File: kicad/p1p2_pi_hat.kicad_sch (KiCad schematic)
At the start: 68 parts, among them J1 Raspberry_Pi_2_3, J2 PC MC_1,5_2-G-3.81, Q1 BSS123, SW1 SW_Push, U1 LM4040DBZ-3, U103 TS4990, U3 Pico

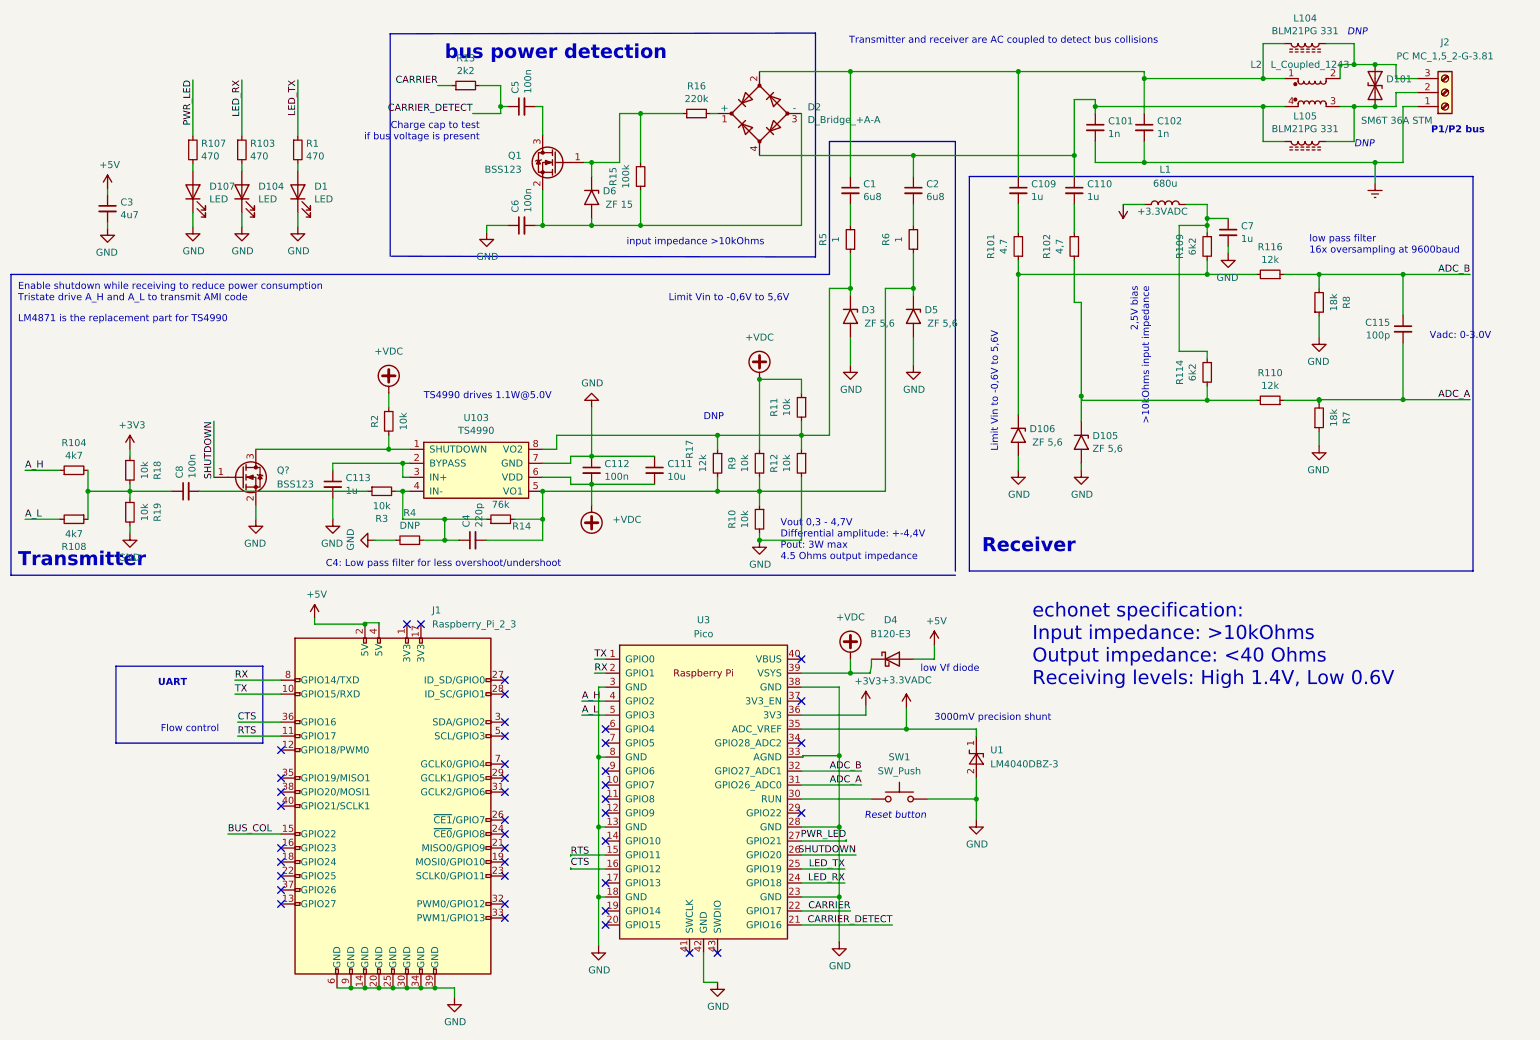
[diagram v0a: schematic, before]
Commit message: kicad: use DNP flag
Signed-off-by: Patrick Rudolph <rudolphpatrick05@gmail.com>
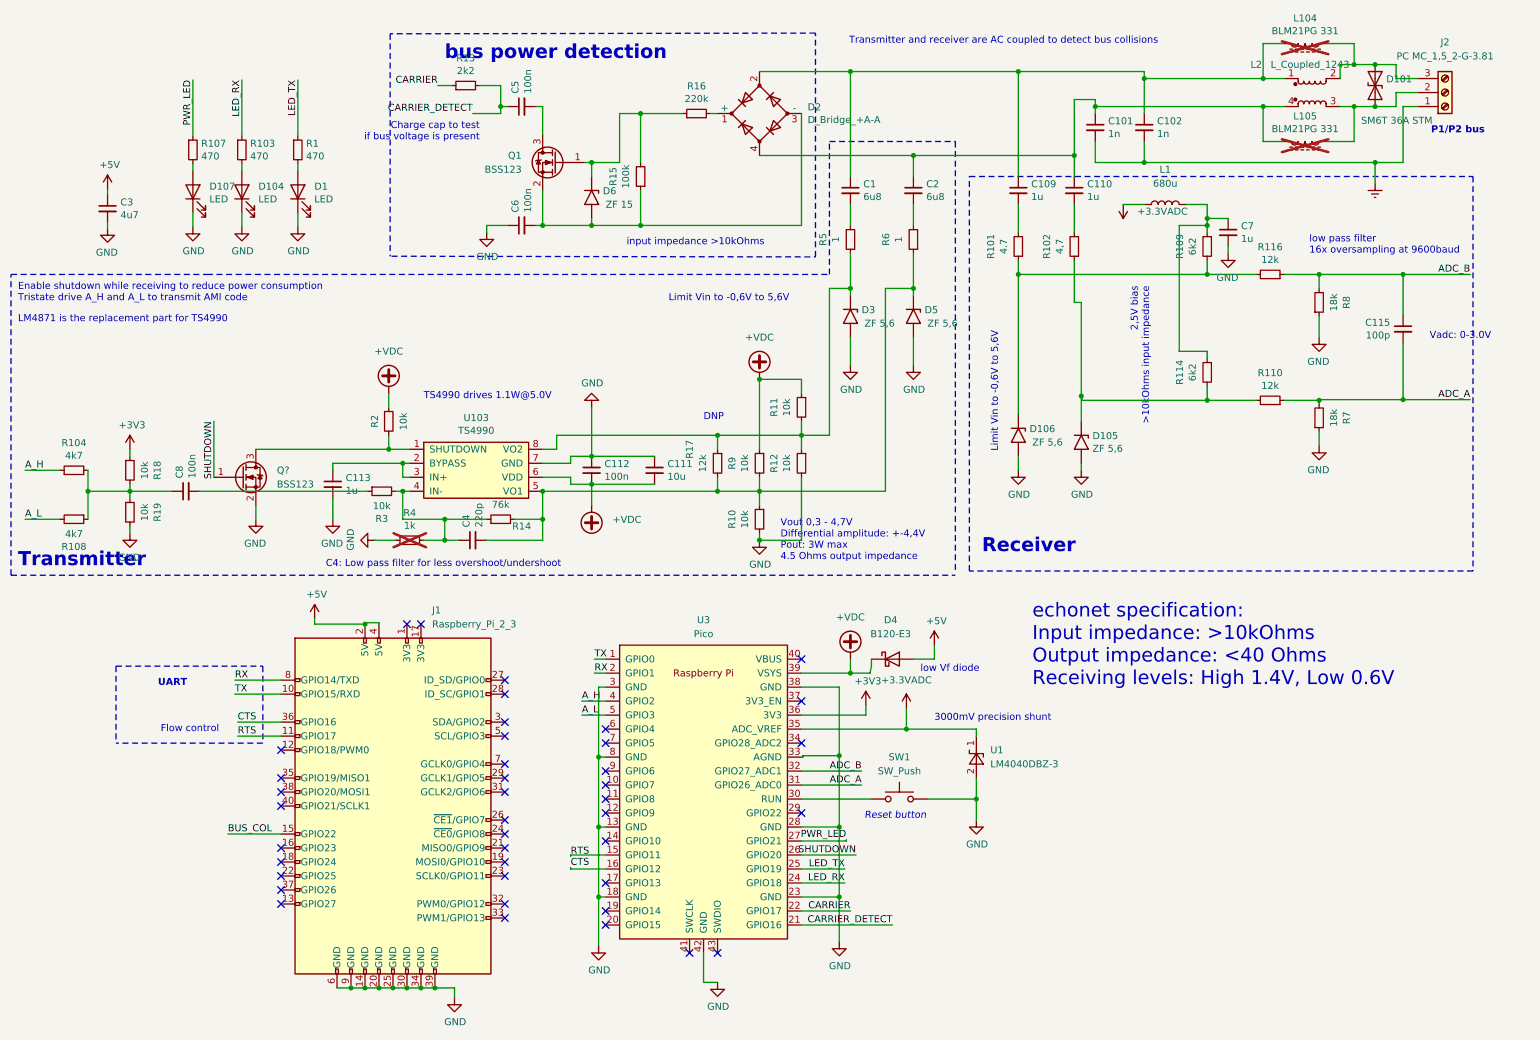
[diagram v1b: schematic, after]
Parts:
- L104, L105: now not fitted
- R4: value DNP -> 1k; now not fitted
